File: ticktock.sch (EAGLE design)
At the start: 47 parts, among them IC1 ATMEGA644A, IC2 AD8611R, IC3 REF200U, J1 AVR_SPI_PRG_6NS, Q1 MOSFET-NCHANNEL2N7002PW, Q2 MOSFET-NCHANNELBSS138, Q3 MOSFET-NCHANNELBSS138, U1 MAX232SOIC16, U2 OSCILLATORSMD, U3 FT232RLSSOP, U4 BMP180

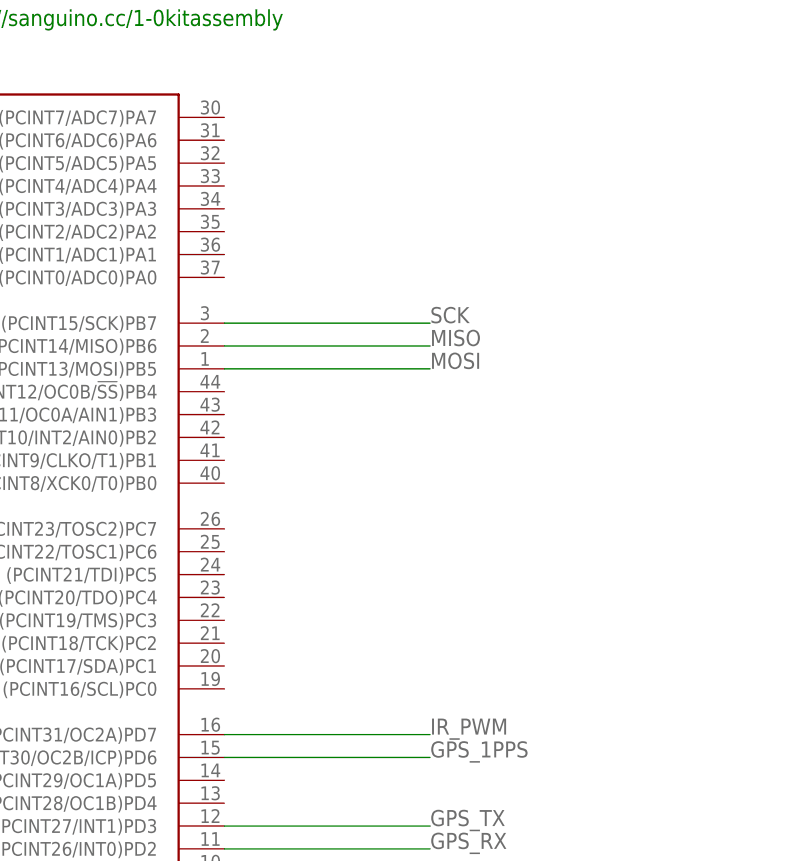
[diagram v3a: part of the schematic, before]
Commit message: wire up analog inputs and I2C to MCU
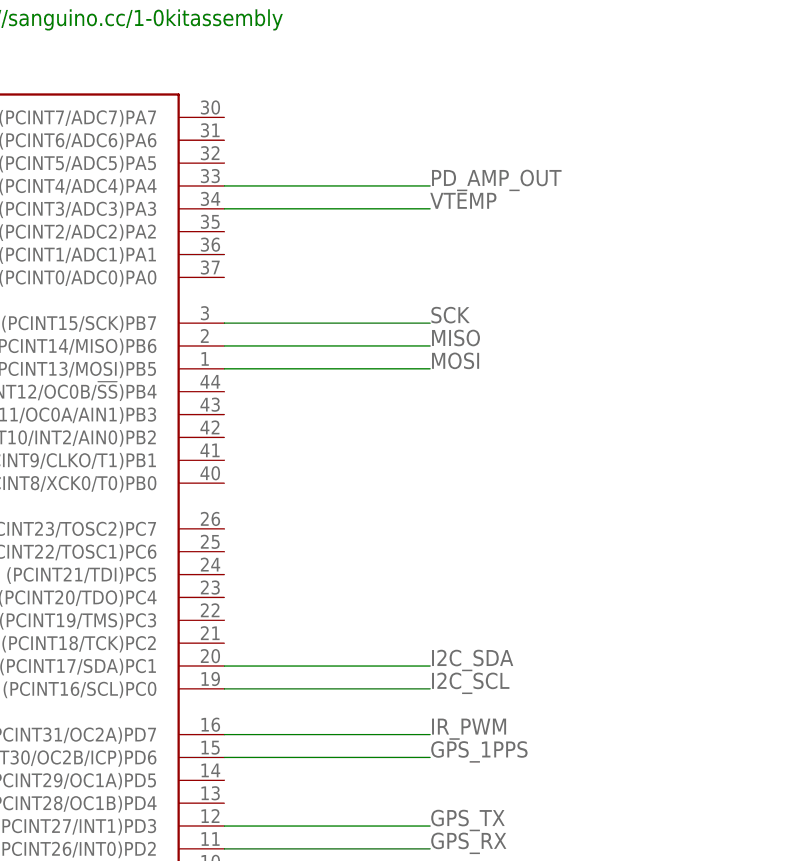
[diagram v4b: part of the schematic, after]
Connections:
- net I2C_SCL: now also IC1.(PCINT16/SCL)PC0
- net I2C_SDA: now also IC1.(PCINT17/SDA)PC1
- net PD_AMP_OUT: now also IC1.(PCINT4/ADC4)PA4
- net VTEMP: now also IC1.(PCINT3/ADC3)PA3
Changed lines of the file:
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@@
 <wire x1="134.62" y1="297.18" x2="134.62" y2="281.94" width="0.1524" layer="91"/>
+</segment>
+<segment>
+<pinref part="IC1" gate="G$1" pin="(PCINT4/ADC4)PA4"/>
+<wire x1="165.1" y1="180.34" x2="187.96" y2="180.34" width="0.1524" layer="91"/>
+<label x="187.96" y="180.34" size="1.778" layer="95"/>
 </segment>
 </net>
@@
 <wire x1="416.56" y1="68.58" x2="416.56" y2="71.12" width="0.1524" layer="91"/>
 <label x="439.42" y="71.12" size="1.778" layer="95"/>
+</segment>
+<segment>
+<pinref part="IC1" gate="G$1" pin="(PCINT3/ADC3)PA3"/>
+<wire x1="165.1" y1="177.8" x2="187.96" y2="177.8" width="0.1524" layer="91"/>
+<label x="187.96" y="177.8" size="1.778" layer="95"/>
 </segment>
 </net>
@@
 <label x="444.5" y="144.78" size="1.778" layer="95"/>
 </segment>
+<segment>
+<pinref part="IC1" gate="G$1" pin="(PCINT16/SCL)PC0"/>
+<wire x1="165.1" y1="124.46" x2="187.96" y2="124.46" width="0.1524" layer="91"/>
+<label x="187.96" y="124.46" size="1.778" layer="95"/>
+</segment>
 </net>
 <net name="N$18" class="0">
@@
 <label x="502.92" y="139.7" size="1.778" layer="95"/>
 </segment>
+<segment>
+<pinref part="IC1" gate="G$1" pin="(PCINT17/SDA)PC1"/>
+<wire x1="165.1" y1="127" x2="187.96" y2="127" width="0.1524" layer="91"/>
+<label x="187.96" y="127" size="1.778" layer="95"/>
+</segment>
 </net>

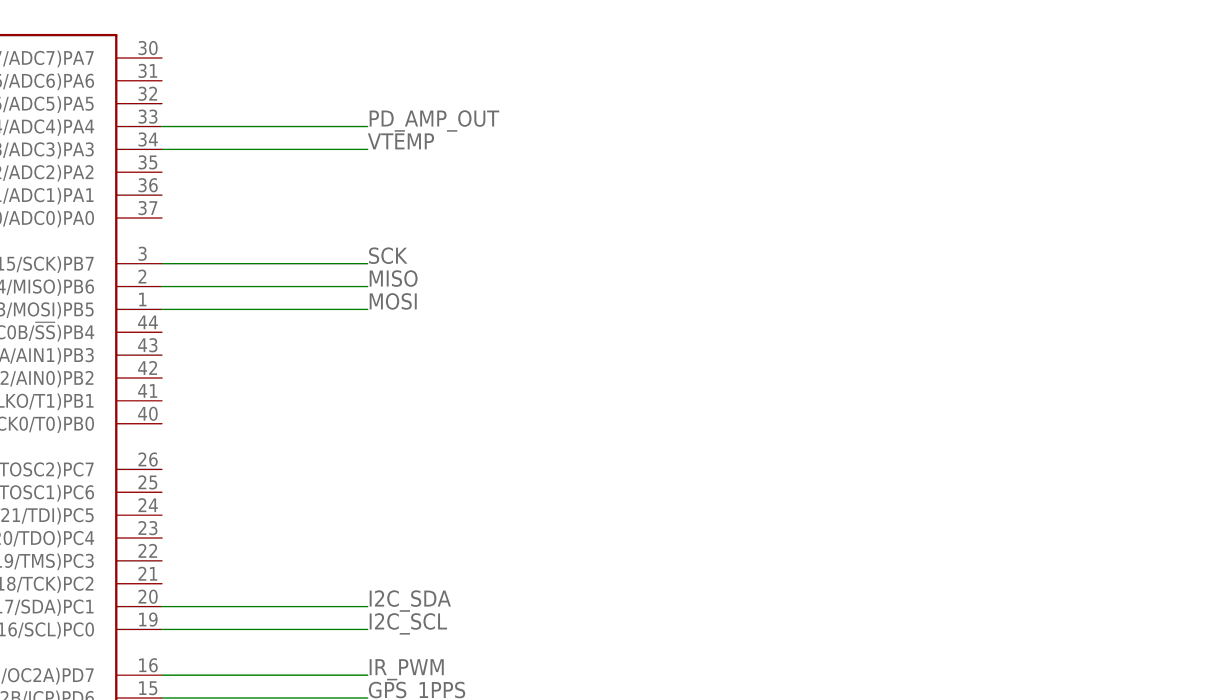
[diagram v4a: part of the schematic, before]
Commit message: Add 3 indicator LEDs
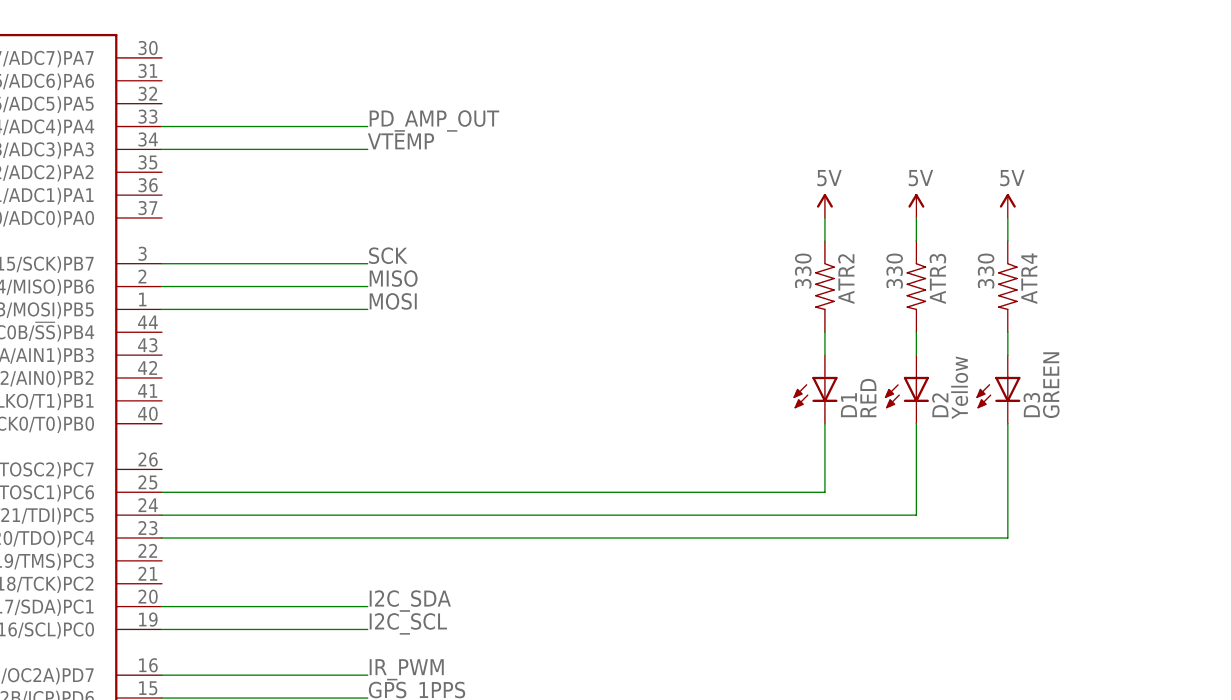
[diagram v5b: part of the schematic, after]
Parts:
- added ATR2, ATR3, ATR4: 330, SparkFun-Resistors:RESISTOR0805-RES
- added D1: RED, SparkFun-LED:LED-REDLILYPAD
- added D2: Yellow, SparkFun-LED:LED-YELLOWLILYPAD
- added D3: GREEN, SparkFun-LED:LED-GREENLILYPAD
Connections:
- new net N$16: ATR2.2, D1.A
- new net N$20: ATR3.2, D2.A
- new net N$21: ATR4.2, D3.A
- new net N$22: D1.C
- new net N$23: D2.C, IC1.(PCINT21/TDI)PC5
- new net N$24: D3.C, IC1.(PCINT20/TDO)PC4
- new net N$25: IC1.(PCINT22/TOSC1)PC6
- net 5V: now also ATR2.1, ATR3.1, ATR4.1
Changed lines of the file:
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@@
 <part name="SUPPLY26" library="SparkFun-Aesthetics" deviceset="5V" device=""/>
 <part name="SUPPLY27" library="SparkFun-Aesthetics" deviceset="5V" device=""/>
+<part name="ATR2" library="SparkFun-Resistors" deviceset="RESISTOR" device="0805-RES" value="330"/>
+<part name="ATR3" library="SparkFun-Resistors" deviceset="RESISTOR" device="0805-RES" value="330"/>
+<part name="ATR4" library="SparkFun-Resistors" deviceset="RESISTOR" device="0805-RES" value="330"/>
+<part name="D2" library="SparkFun-LED" deviceset="LED-YELLOW" device="LILYPAD" value="Yellow"/>
+<part name="D1" library="SparkFun-LED" deviceset="LED-RED" device="LILYPAD" value="RED"/>
+<part name="D3" library="SparkFun-LED" deviceset="LED-GREEN" device="LILYPAD" value="GREEN"/>
+<part name="SUPPLY28" library="SparkFun-Aesthetics" deviceset="5V" device=""/>
+<part name="SUPPLY29" library="SparkFun-Aesthetics" deviceset="5V" device=""/>
+<part name="SUPPLY30" library="SparkFun-Aesthetics" deviceset="5V" device=""/>
 </parts>
 <sheets>
@@
 <instance part="SUPPLY26" gate="G$1" x="429.26" y="180.34"/>
 <instance part="SUPPLY27" gate="G$1" x="487.68" y="180.34"/>
+<instance part="ATR2" gate="G$1" x="238.76" y="162.56" rot="R270"/>
+<instance part="ATR3" gate="G$1" x="248.92" y="162.56" rot="R270"/>
+<instance part="ATR4" gate="G$1" x="259.08" y="162.56" rot="R270"/>
+<instance part="D2" gate="G$1" x="248.92" y="152.4"/>
+<instance part="D1" gate="G$1" x="238.76" y="152.4"/>
+<instance part="D3" gate="G$1" x="259.08" y="152.4"/>
+<instance part="SUPPLY28" gate="G$1" x="238.76" y="170.18"/>
+<instance part="SUPPLY29" gate="G$1" x="248.92" y="170.18"/>
+<instance part="SUPPLY30" gate="G$1" x="259.08" y="170.18"/>
 </instances>
 <busses>
@@
 <wire x1="487.68" y1="160.02" x2="487.68" y2="180.34" width="0.1524" layer="91"/>
 </segment>
+<segment>
+<pinref part="SUPPLY28" gate="G$1" pin="5V"/>
+<pinref part="ATR2" gate="G$1" pin="1"/>
+<wire x1="238.76" y1="170.18" x2="238.76" y2="167.64" width="0.1524" layer="91"/>
+</segment>
+<segment>
+<pinref part="SUPPLY29" gate="G$1" pin="5V"/>
+<pinref part="ATR3" gate="G$1" pin="1"/>
+<wire x1="248.92" y1="170.18" x2="248.92" y2="167.64" width="0.1524" layer="91"/>
+</segment>
+<segment>
+<pinref part="SUPPLY30" gate="G$1" pin="5V"/>
+<pinref part="ATR4" gate="G$1" pin="1"/>
+<wire x1="259.08" y1="170.18" x2="259.08" y2="167.64" width="0.1524" layer="91"/>
+</segment>
 </net>
 <net name="N$1" class="0">
@@
 </segment>
 </net>
+<net name="N$16" class="0">
+<segment>
+<pinref part="ATR2" gate="G$1" pin="2"/>
+<pinref part="D1" gate="G$1" pin="A"/>
+<wire x1="238.76" y1="157.48" x2="238.76" y2="154.94" width="0.1524" layer="91"/>
+</segment>
+</net>
+<net name="N$20" class="0">
+<segment>
+<pinref part="ATR3" gate="G$1" pin="2"/>
+<pinref part="D2" gate="G$1" pin="A"/>
+<wire x1="248.92" y1="157.48" x2="248.92" y2="154.94" width="0.1524" layer="91"/>
+</segment>
+</net>
+<net name="N$21" class="0">
+<segment>
+<pinref part="ATR4" gate="G$1" pin="2"/>
+<pinref part="D3" gate="G$1" pin="A"/>
+<wire x1="259.08" y1="157.48" x2="259.08" y2="154.94" width="0.1524" layer="91"/>
+</segment>
+</net>
+<net name="N$22" class="0">
+<segment>
+<pinref part="D1" gate="G$1" pin="C"/>
+<wire x1="238.76" y1="147.32" x2="238.76" y2="139.7" width="0.1524" layer="91"/>
+</segment>
+</net>
+<net name="N$23" class="0">
+<segment>
+<pinref part="D2" gate="G$1" pin="C"/>
+<wire x1="248.92" y1="147.32" x2="248.92" y2="137.16" width="0.1524" layer="91"/>
+<pinref part="IC1" gate="G$1" pin="(PCINT21/TDI)PC5"/>
+<wire x1="248.92" y1="137.16" x2="165.1" y2="137.16" width="0.1524" layer="91"/>
+</segment>
+</net>
+<net name="N$24" class="0">
+<segment>
+<pinref part="D3" gate="G$1" pin="C"/>
+<wire x1="259.08" y1="147.32" x2="259.08" y2="134.62" width="0.1524" layer="91"/>
+<pinref part="IC1" gate="G$1" pin="(PCINT20/TDO)PC4"/>
+<wire x1="165.1" y1="134.62" x2="259.08" y2="134.62" width="0.1524" layer="91"/>
+</segment>
+</net>
+<net name="N$25" class="0">
+<segment>
+<pinref part="IC1" gate="G$1" pin="(PCINT22/TOSC1)PC6"/>
+<wire x1="165.1" y1="139.7" x2="238.76" y2="139.7" width="0.1524" layer="91"/>
+</segment>
+</net>
